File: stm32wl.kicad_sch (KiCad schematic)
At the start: 24 parts, among them U201 STM32WLE5CCUx

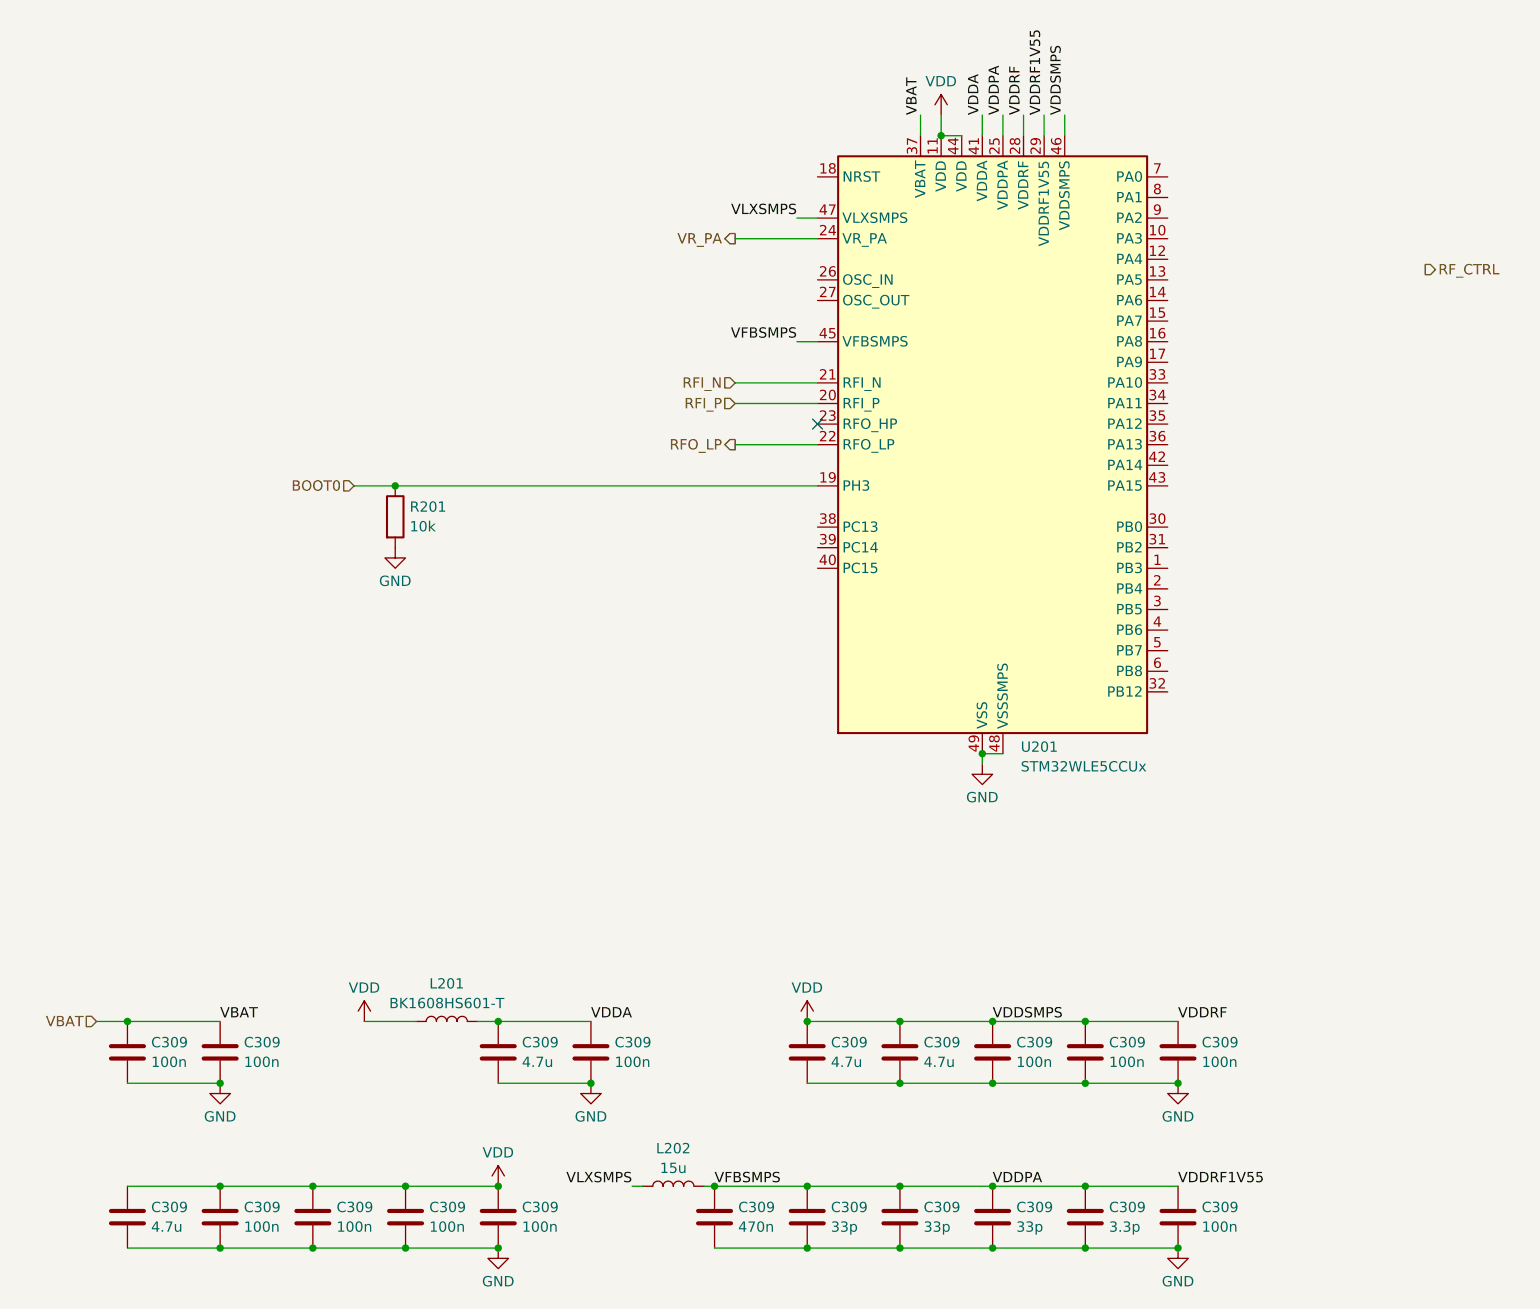
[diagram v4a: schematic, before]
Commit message: added tag-connect and a led, noticed i forgot a crystal
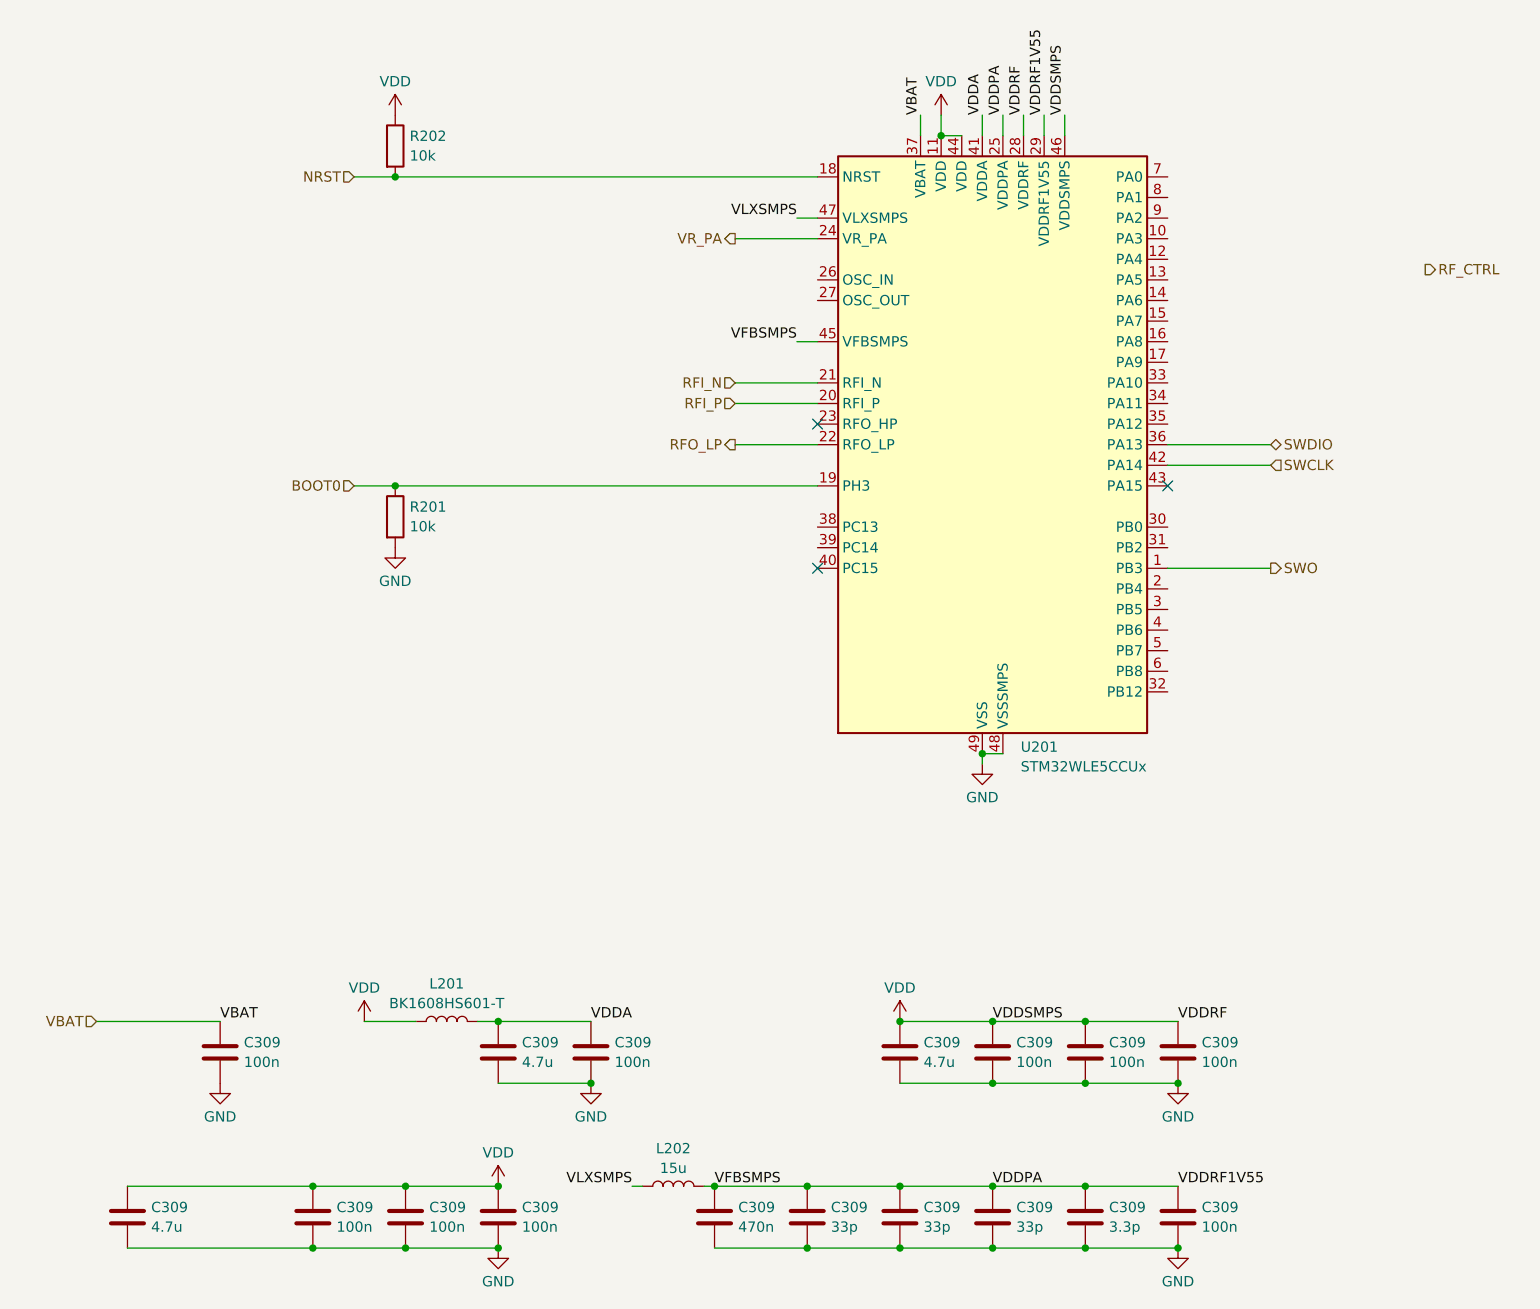
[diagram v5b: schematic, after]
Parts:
- removed C309: 4.7u, Capacitor_SMD:C_0603_1608Metric, symbol Device:C
- removed C309 (x2): 100n, Capacitor_SMD:C_0402_1005Metric, symbol Device:C
- added R202: 10k, Resistor_SMD:R_0402_1005Metric, symbol Device:R
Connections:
- net VDD: now also R202.1
- net SWO: now reaches U201.1 (PB3)
- net NRST: now reaches U201.18 (NRST)
- net NRST: now also R202.2
- net SWDIO: now reaches U201.36 (PA13)
- net SWCLK: now reaches U201.42 (PA14)
- no-connect marks 1 -> 3

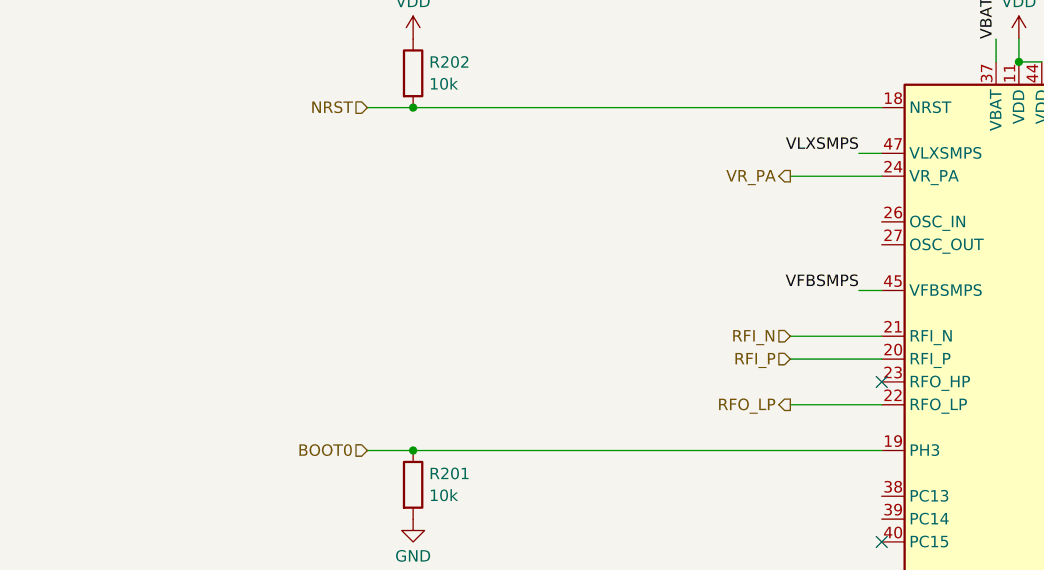
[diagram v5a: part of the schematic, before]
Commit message: added the crystal
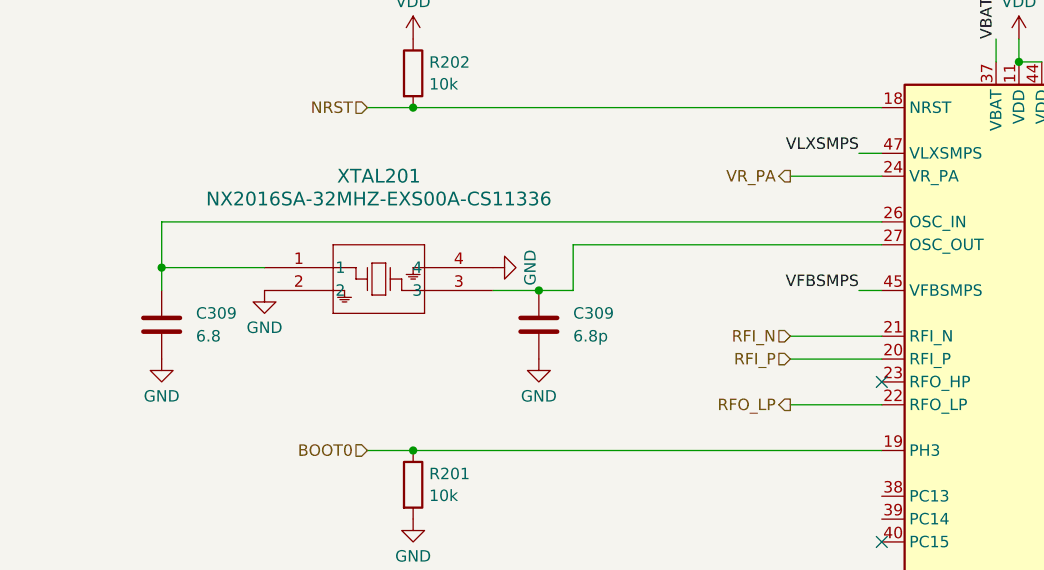
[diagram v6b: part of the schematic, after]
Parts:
- added C309: 6.8p, Capacitor_SMD:C_0402_1005Metric, symbol Device:C
- added C309: 6.8, Capacitor_SMD:C_0402_1005Metric, symbol Device:C
- added XTAL201: NX2016SA-32MHZ-EXS00A-CS11336, NX2016SA_NDK, symbol NX2016SA_NDK-CS11336-32M:NX2016SA-32MHZ-EXS00A-CS11336
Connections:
- net GND: now also C309.1, C309.2, XTAL201.2, XTAL201.4
- net at U201.26 (OSC_IN): now also C309.2, XTAL201.1
- net at U201.27 (OSC_OUT): now also C309.1, XTAL201.3

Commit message: added castellated edge connectors
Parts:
- XTAL201: footprint NX2016SA_NDK -> lora-module:NX2016SA_NDK
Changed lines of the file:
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@@
       (effects (font (size 1.524 1.524)))
     )
-    (property "Footprint" "NX2016SA_NDK" (at 46.99 74.93 0)
+    (property "Footprint" "lora-module:NX2016SA_NDK" (at 46.99 74.93 0)
       (effects (font (size 1.27 1.27) italic) hide)
     )

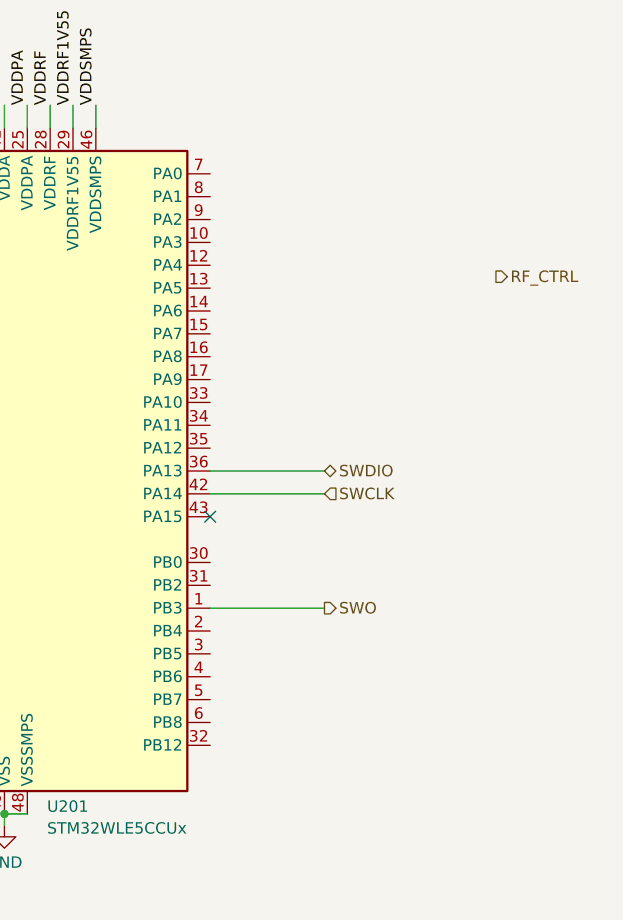
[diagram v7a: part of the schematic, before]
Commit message: created a footprint for the edge connectors
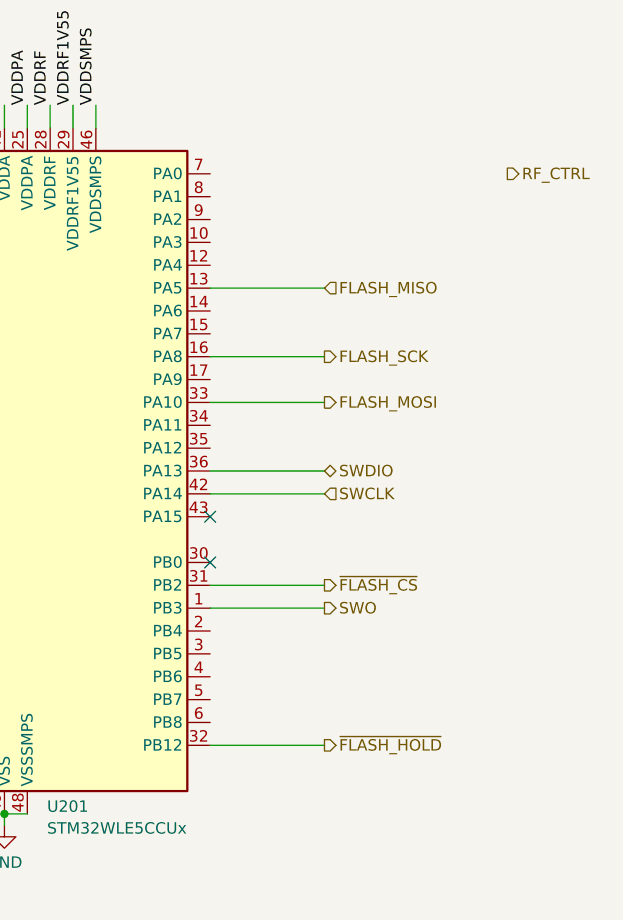
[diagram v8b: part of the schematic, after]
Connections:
- net FLASH_MISO: now reaches U201.13 (PA5)
- net FLASH_SCK: now reaches U201.16 (PA8)
- net ~{FLASH_CS}: now reaches U201.31 (PB2)
- net ~{FLASH_HOLD}: now reaches U201.32 (PB12)
- net FLASH_MOSI: now reaches U201.33 (PA10)
- no-connect marks 3 -> 4
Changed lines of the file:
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@@
   (no_connect (at 115.57 87.63))
   (no_connect (at 158.75 95.25))
+  (no_connect (at 158.75 100.33))
   (wire (pts (xy 35.56 74.93) (xy 35.56 69.85))
     (stroke (width 0) (type default))
@@
     (stroke (width 0) (type default))
   )
+  (wire (pts (xy 158.75 82.55) (xy 171.45 82.55))
+    (stroke (width 0) (type default))
+  )
   (wire (pts (xy 77.47 77.47) (xy 81.28 77.47))
     (stroke (width 0) (type default))
@@
     (stroke (width 0) (type default))
   )
+  (wire (pts (xy 158.75 69.85) (xy 171.45 69.85))
+    (stroke (width 0) (type default))
+  )
   (wire (pts (xy 92.71 181.61) (xy 93.98 181.61))
     (stroke (width 0) (type default))
@@
     (stroke (width 0) (type default))
   )
+  (wire (pts (xy 158.75 77.47) (xy 171.45 77.47))
+    (stroke (width 0) (type default))
+  )
   (wire (pts (xy 137.16 181.61) (xy 148.59 181.61))
     (stroke (width 0) (type default))
@@
     (stroke (width 0) (type default))
   )
+  (wire (pts (xy 158.75 102.87) (xy 171.45 102.87))
+    (stroke (width 0) (type default))
+  )
   (wire (pts (xy 158.75 105.41) (xy 171.45 105.41))
     (stroke (width 0) (type default))
@@
   )
   (wire (pts (xy 158.75 92.71) (xy 171.45 92.71))
+    (stroke (width 0) (type default))
+  )
+  (wire (pts (xy 158.75 120.65) (xy 171.45 120.65))
     (stroke (width 0) (type default))
   )
@@
     (effects (font (size 1.27 1.27)) (justify left bottom))
   )
+  (hierarchical_label "~{FLASH_CS}" (shape output) (at 171.45 102.87 0) (fields_autoplaced)
+    (effects (font (size 1.27 1.27)) (justify left))
+  )
   (hierarchical_label "RFI_P" (shape input) (at 105.41 85.09 180) (fields_autoplaced)
     (effects (font (size 1.27 1.27)) (justify right))
@@
     (effects (font (size 1.27 1.27)) (justify right))
   )
-  (hierarchical_label "RF_CTRL" (shape output) (at 190.5 68.58 0) (fields_autoplaced)
+  (hierarchical_label "RF_CTRL" (shape output) (at 191.77 57.15 0) (fields_autoplaced)
+    (effects (font (size 1.27 1.27)) (justify left))
+  )
+  (hierarchical_label "FLASH_MOSI" (shape output) (at 171.45 82.55 0) (fields_autoplaced)
+    (effects (font (size 1.27 1.27)) (justify left))
+  )
+  (hierarchical_label "FLASH_MISO" (shape input) (at 171.45 69.85 0) (fields_autoplaced)
+    (effects (font (size 1.27 1.27)) (justify left))
+  )
+  (hierarchical_label "~{FLASH_HOLD}" (shape output) (at 171.45 120.65 0) (fields_autoplaced)
     (effects (font (size 1.27 1.27)) (justify left))
   )
@@
     (effects (font (size 1.27 1.27)) (justify right))
   )
+  (hierarchical_label "FLASH_SCK" (shape output) (at 171.45 77.47 0) (fields_autoplaced)
+    (effects (font (size 1.27 1.27)) (justify left))
+  )
   (hierarchical_label "BOOT0" (shape input) (at 58.42 95.25 180) (fields_autoplaced)
